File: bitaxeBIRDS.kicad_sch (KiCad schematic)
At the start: 10 parts, among them J1 XT30

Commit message: fix part numbers for C60-C64 for #5
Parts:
- HS1: footprint bitaxe:Heatsink-BitaxeGT -> bitaxe:Heatsink-5hole-BitaxeGT
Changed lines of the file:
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@@
 			)
 		)
-		(property "Footprint" "bitaxe:Heatsink-BitaxeGT"
+		(property "Footprint" "bitaxe:Heatsink-5hole-BitaxeGT"
 			(at 122.2248 179.07 0)
 			(effects

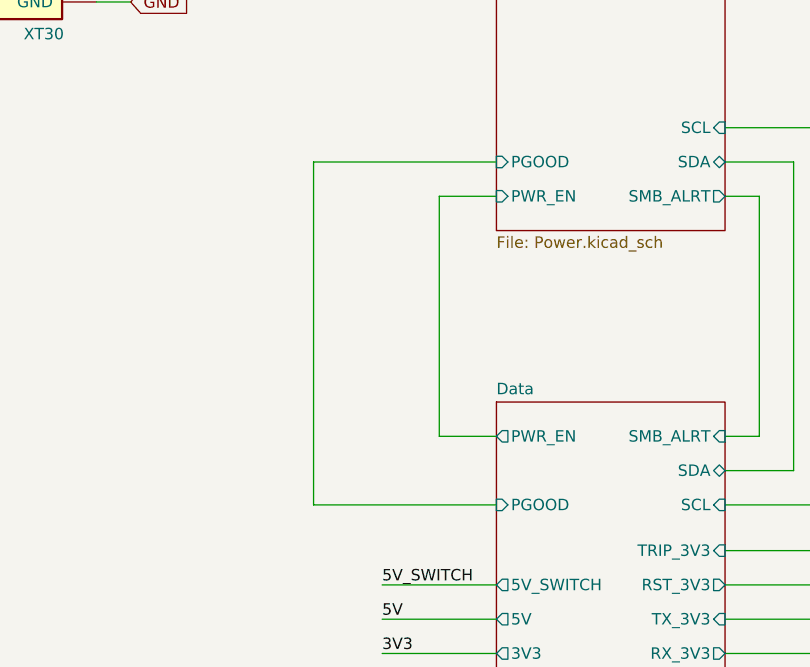
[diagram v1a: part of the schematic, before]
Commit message: added pull resistors for #1
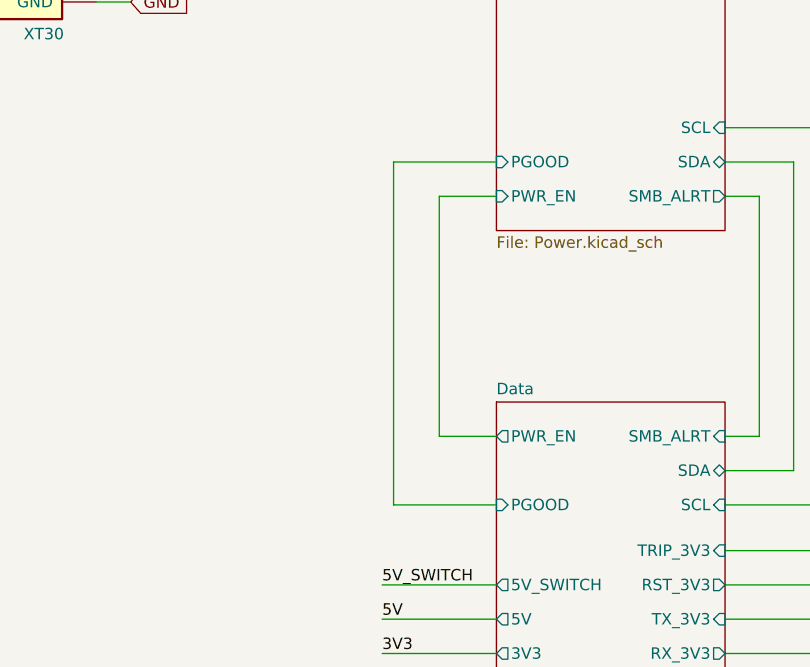
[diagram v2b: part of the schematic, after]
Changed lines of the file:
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@@
 	(wire
 		(pts
-			(xy 82.55 66.04) (xy 82.55 104.14)
+			(xy 91.44 66.04) (xy 91.44 104.14)
 		)
 		(stroke
@@
 	(wire
 		(pts
-			(xy 82.55 104.14) (xy 102.87 104.14)
+			(xy 91.44 104.14) (xy 102.87 104.14)
 		)
 		(stroke
@@
 	(wire
 		(pts
-			(xy 82.55 66.04) (xy 102.87 66.04)
-		)
-		(stroke
+			(xy 91.44 66.04) (xy 102.87 66.04)
+		)
+		(stroke
